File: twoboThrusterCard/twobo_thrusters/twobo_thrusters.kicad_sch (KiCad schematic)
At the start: 14 parts, among them J2 Conn_01x09, J5 Conn_02x40_Odd_Even

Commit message: Thruster card
added the stack up connector.
first iteration of routing
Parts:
- J5: footprint Samtec Custom:Samtec_HLE-140-02-L-DV-PE_2x40_P2.54mm_Horizontal -> custom_components:Samtec_HLE-140-02-L-DV-PE_2x40_P2.54mm_Horizontal
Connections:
- net +3V3 is gone; now on net +3.3V: J5.65 (Pin_65), J5.67 (Pin_67), J5.69 (Pin_69)
- net +3.3V: now also A1.1 (A), A2.1 (A), A3.1 (A)
- net +5V: no longer A1.1 (A), A2.1 (A), A3.1 (A)
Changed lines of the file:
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@@
 			)
 		)
-		(property "Value" "+3V3"
+		(property "Value" "+3.3V"
 			(at 133.35 119.3799 90)
 			(effects
@@
 			)
 		)
-		(property "Value" "+5V"
-			(at 45.72 90.17 90)
+		(property "Value" "+3.3V"
+			(at 45.72 90.1699 90)
 			(effects
 				(font
@@
 			)
 		)
-		(property "Footprint" "Samtec Custom:Samtec_HLE-140-02-L-DV-PE_2x40_P2.54mm_Horizontal"
+		(property "Footprint" "custom_components:Samtec_HLE-140-02-L-DV-PE_2x40_P2.54mm_Horizontal"
 			(at 147.32 83.82 0)
 			(effects

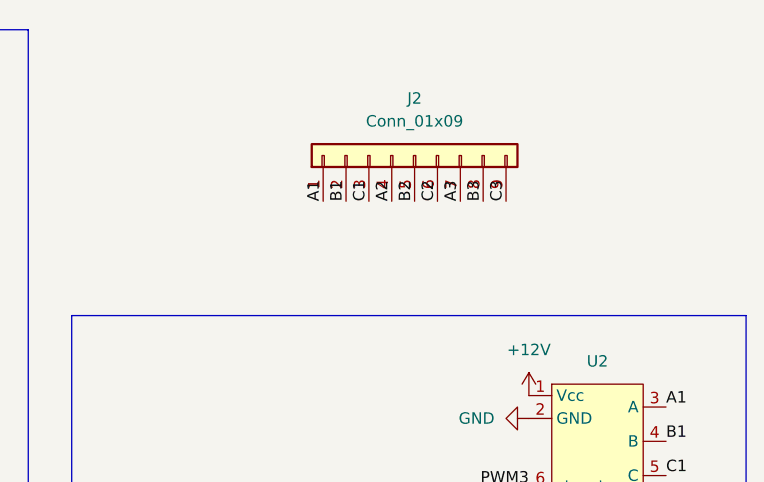
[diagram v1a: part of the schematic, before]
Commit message: Repositioned Thruster Board Connector
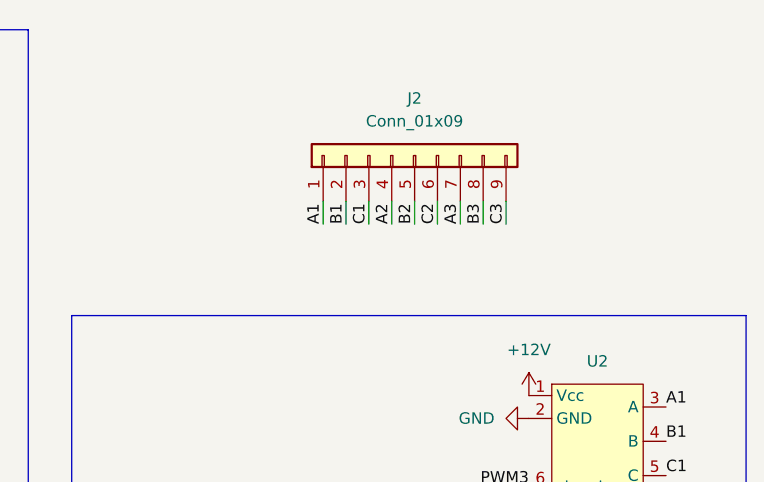
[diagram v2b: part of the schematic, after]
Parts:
- J2: footprint Connector_Molex:Molex_Micro-Fit_3.0_43650-0915_1x09_P3.00mm_Vertical -> Connector_Molex:Molex_Micro-Fit_3.0_43650-0900_1x09_P3.00mm_Horizontal
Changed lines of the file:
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@@
+	(wire
+		(pts
+			(xy 227.33 50.8) (xy 227.33 48.26)
+		)
+		(stroke
+			(width 0)
+			(type default)
+		)
+	)
 	(wire
 		(pts
@@
 	(wire
 		(pts
+			(xy 237.49 50.8) (xy 237.49 48.26)
+		)
+		(stroke
+			(width 0)
+			(type default)
+		)
+	)
+	(wire
+		(pts
 			(xy 87.63 74.93) (xy 91.44 74.93)
 		)
@@
 	(wire
 		(pts
+			(xy 234.95 50.8) (xy 234.95 48.26)
+		)
+		(stroke
+			(width 0)
+			(type default)
+		)
+	)
+	(wire
+		(pts
 			(xy 40.64 73.66) (xy 40.64 72.39)
 		)
@@
 	(wire
 		(pts
+			(xy 217.17 50.8) (xy 217.17 48.26)
+		)
+		(stroke
+			(width 0)
+			(type default)
+		)
+	)
+	(wire
+		(pts
 			(xy 137.16 119.38) (xy 142.24 119.38)
 		)
@@
 	(wire
 		(pts
+			(xy 219.71 50.8) (xy 219.71 48.26)
+		)
+		(stroke
+			(width 0)
+			(type default)
+		)
+	)
+	(wire
+		(pts
 			(xy 142.24 99.06) (xy 142.24 101.6)
 		)
@@
 	(wire
 		(pts
+			(xy 224.79 50.8) (xy 224.79 48.26)
+		)
+		(stroke
+			(width 0)
+			(type default)
+		)
+	)
+	(wire
+		(pts
 			(xy 40.64 87.63) (xy 66.04 87.63)
 		)
@@
 	(wire
 		(pts
+			(xy 222.25 50.8) (xy 222.25 48.26)
+		)
+		(stroke
+			(width 0)
+			(type default)
+		)
+	)
+	(wire
+		(pts
 			(xy 40.64 97.79) (xy 66.04 97.79)
 		)
@@
 	(wire
 		(pts
+			(xy 229.87 50.8) (xy 229.87 48.26)
+		)
+		(stroke
+			(width 0)
+			(type default)
+		)
+	)
+	(wire
+		(pts
 			(xy 40.64 107.95) (xy 66.04 107.95)
 		)
@@
 	(wire
 		(pts
+			(xy 232.41 50.8) (xy 232.41 48.26)
+		)
+		(stroke
+			(width 0)
+			(type default)
+		)
+	)
+	(wire
+		(pts
 			(xy 87.63 92.71) (xy 90.17 92.71)
 		)
@@
 	)
 	(label "B3"
-		(at 234.95 48.26 90)
+		(at 234.95 50.8 90)
 		(effects
 			(font
@@
 	)
 	(label "A3"
-		(at 232.41 48.26 90)
+		(at 232.41 50.8 90)
 		(effects
 			(font
@@
 	)
 	(label "A1"
-		(at 217.17 48.26 90)
+		(at 217.17 50.8 90)
 		(effects
 			(font
@@
 	)
 	(label "C2"
-		(at 229.87 48.26 90)
+		(at 229.87 50.8 90)
 		(effects
 			(font
@@
 	)
 	(label "B2"
-		(at 227.33 48.26 90)
+		(at 227.33 50.8 90)
 		(effects
 			(font
@@
 	)
 	(label "B1"
-		(at 219.71 48.26 90)
+		(at 219.71 50.8 90)
 		(effects
 			(font
@@
 	)
 	(label "A2"
-		(at 224.79 48.26 90)
+		(at 224.79 50.8 90)
 		(effects
 			(font
@@
 	)
 	(label "C3"
-		(at 237.49 48.26 90)
+		(at 237.49 50.8 90)
 		(effects
 			(font
@@
 	)
 	(label "C1"
-		(at 222.25 48.26 90)
+		(at 222.25 50.8 90)
 		(effects
 			(font
@@
 			)
 		)
-		(property "Footprint" "Connector_Molex:Molex_Micro-Fit_3.0_43650-0915_1x09_P3.00mm_Vertical"
+		(property "Footprint" "Connector_Molex:Molex_Micro-Fit_3.0_43650-0900_1x09_P3.00mm_Horizontal"
 			(at 227.33 43.18 0)
 			(effects

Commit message: Viewed Files
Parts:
- added H1, H2, H3, H4: MountingHole, MountingHole:MountingHole_2.2mm_M2, symbol Mechanical:MountingHole
- J5: footprint custom_components:Samtec_HLE-140-02-L-DV-PE_2x40_P2.54mm_Horizontal -> Samtec Custom:Samtec_HLE-140-02-L-DV-PE_2x40_P2.54mm_Horizontal
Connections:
- no-connect marks 10 -> 62
